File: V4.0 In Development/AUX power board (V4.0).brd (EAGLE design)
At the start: 100 x 100 mm, 96 parts, among them U1 ATMEGA328P_TQFP, U2 TPS5405DR

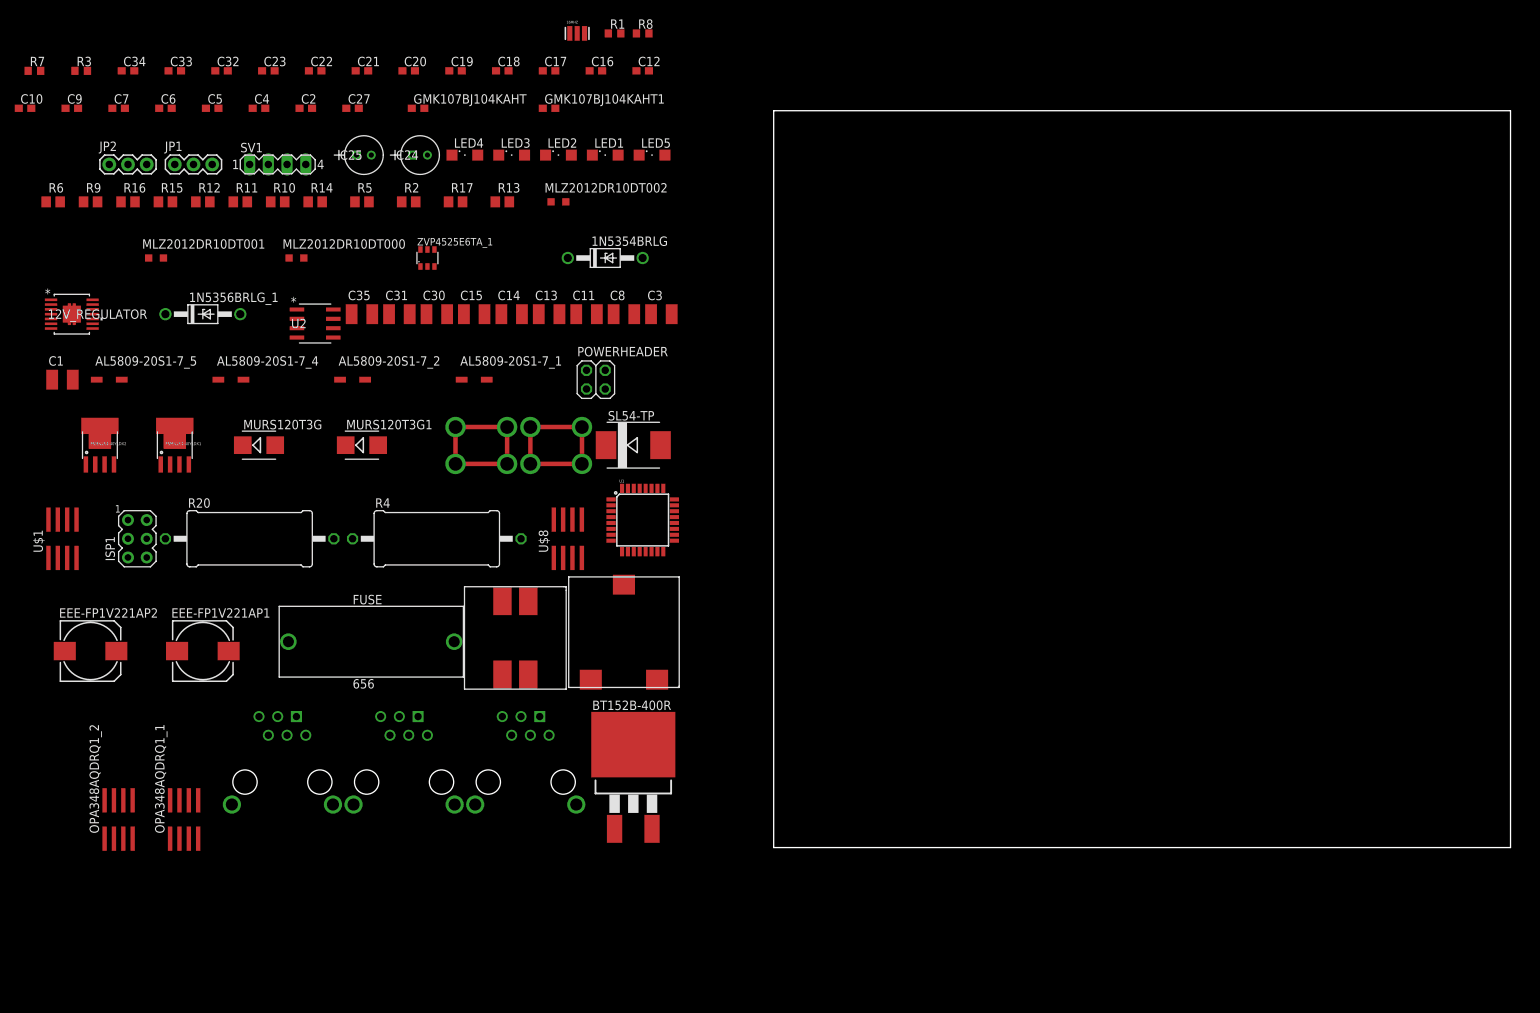
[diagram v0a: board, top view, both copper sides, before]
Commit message: Generated the board file
-Generated Board files
-Sorted the components
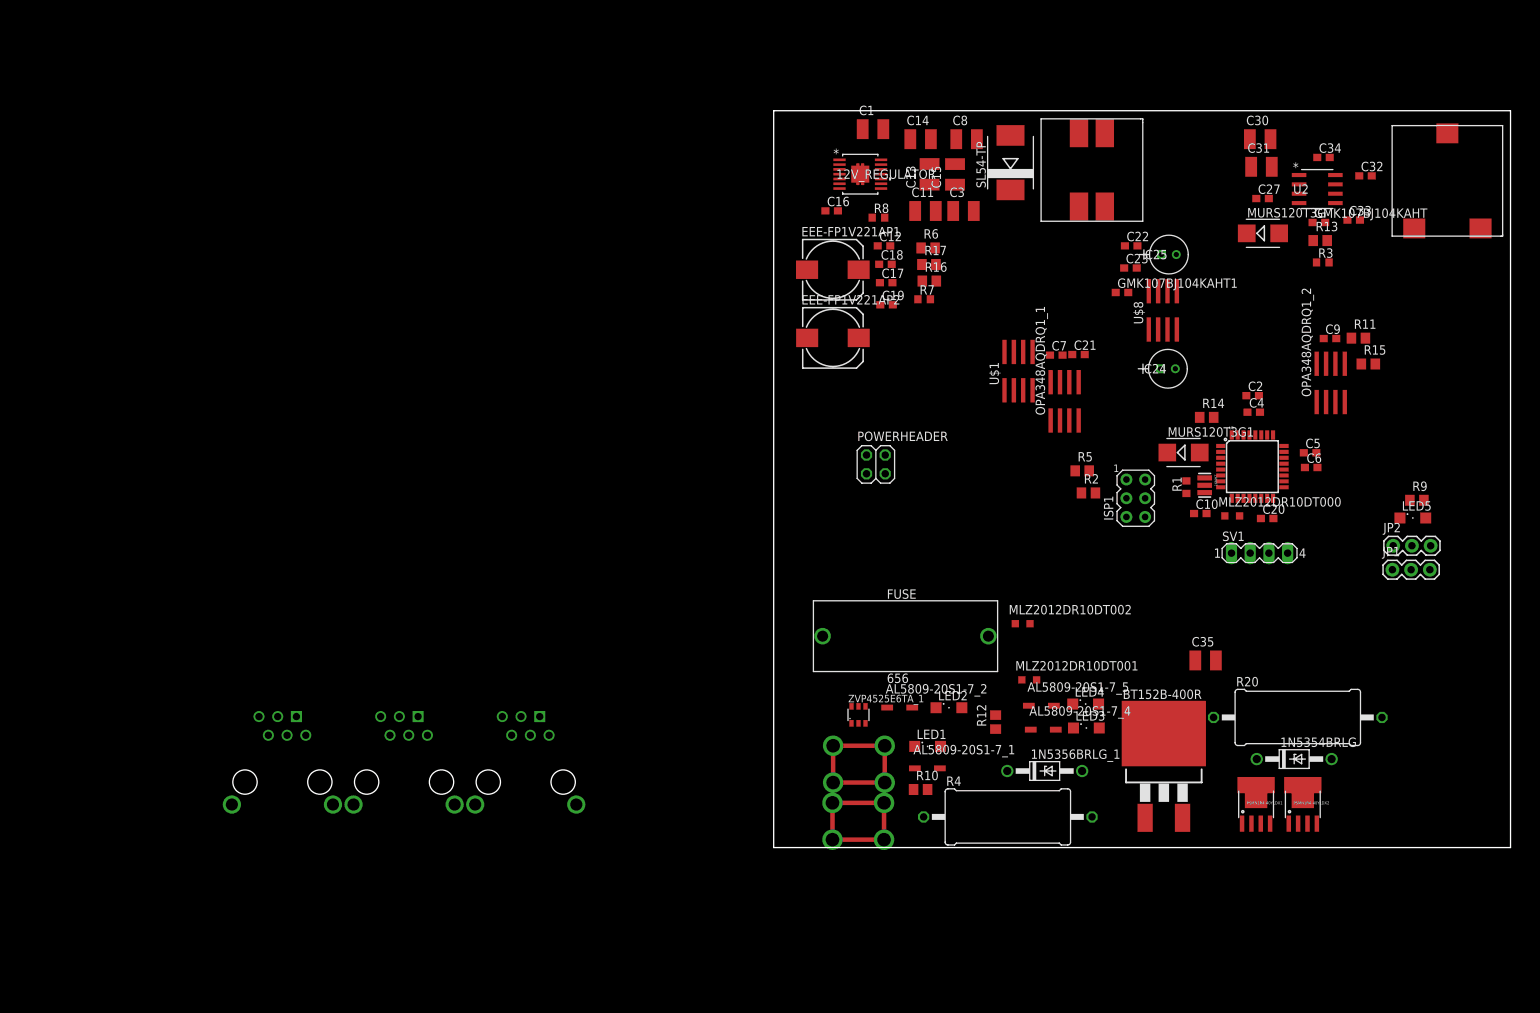
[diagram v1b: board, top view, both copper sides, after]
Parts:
- moved R9 184.5 mm to (87.3, 47.1)
- moved JP2 181.8 mm to (84.1, 41.0)
- moved OPA348AQDRQ1_2 174.8 mm to (75.6, 63.1)
- moved JP1 174.2 mm to (84.0, 37.7)
- moved C9 173.6 mm to (75.5, 69.1)
- moved R3 170.5 mm to (74.5, 79.4)
- moved PSMN1R4-40YLDX2 170.4 mm to (71.8, 5.86)
- moved C10 168.7 mm to (57.9, 45.3)
- moved R15 164.7 mm to (80.7, 65.6)
- moved C6 163.0 mm to (73.0, 51.6)
- moved C34 162.7 mm to (74.6, 93.7)
- moved C33 161.3 mm to (78.7, 85.2)
- moved C5 156.2 mm to (72.8, 53.6)
- moved C32 155.9 mm to (80.3, 91.2)
- moved PSMN1R4-40YLDX1 154.6 mm to (65.5, 5.86)
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
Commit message: Worked on PCB (Input)
-Not complete
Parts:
- moved U$3 108.0 mm to (75.0, 11.7)
- moved U$4 107.0 mm to (57.5, 11.7)
- moved U$10 106.0 mm to (40.0, 11.7)
- moved U$7 80.0 mm to (88.0, 5.00)
- moved LED4 69.5 mm to (-24.7, 38.0)
- moved AL5809-20S1-7_5 68.9 mm to (-26.7, -8.75)
- moved C35 68.6 mm to (-6.38, 3.39)
- moved R12 61.8 mm to (-30.4, 29.5)
- moved LED3 61.0 mm to (-18.6, 17.7)
- moved R4 59.0 mm to (-27.2, 2.66)
- moved MLZ2012DR10DT001 55.5 mm to (-20.8, 24.3)
- moved 1N5356BRLG_1 54.0 mm to (-17.2, 10.4)
- moved R10 49.7 mm to (-29.6, 12.4)
- moved AL5809-20S1-7_4 49.5 mm to (-8.91, -3.50)
- moved MLZ2012DR10DT002 46.2 mm to (-11.7, 22.4)
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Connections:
- net GND: no longer U$10.SH1, U$10.SH2, U$3.SH1, U$3.SH2, U$4.SH1, U$4.SH2
- net NEG_TERMINAL: now also U$10.SH1, U$10.SH2, U$3.SH1, U$3.SH2, U$4.SH1, U$4.SH2
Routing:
- net NEG_TERMINAL: track 0.00 -> 164.9 mm
- net INPUT_UNREG: track 0.00 -> 61.6 mm, vias 0 -> 3
- net N$17: track 0.00 -> 15.8 mm, vias 0 -> 1
- net BATTERY_IN_UNFUSED+: track 0.00 -> 11.4 mm
- net N$25: track 0.00 -> 2.77 mm
- net N$22: track 0.00 -> 2.63 mm
- added copper zone on layer 1, net GND
- added copper zone on layer 16, net GND

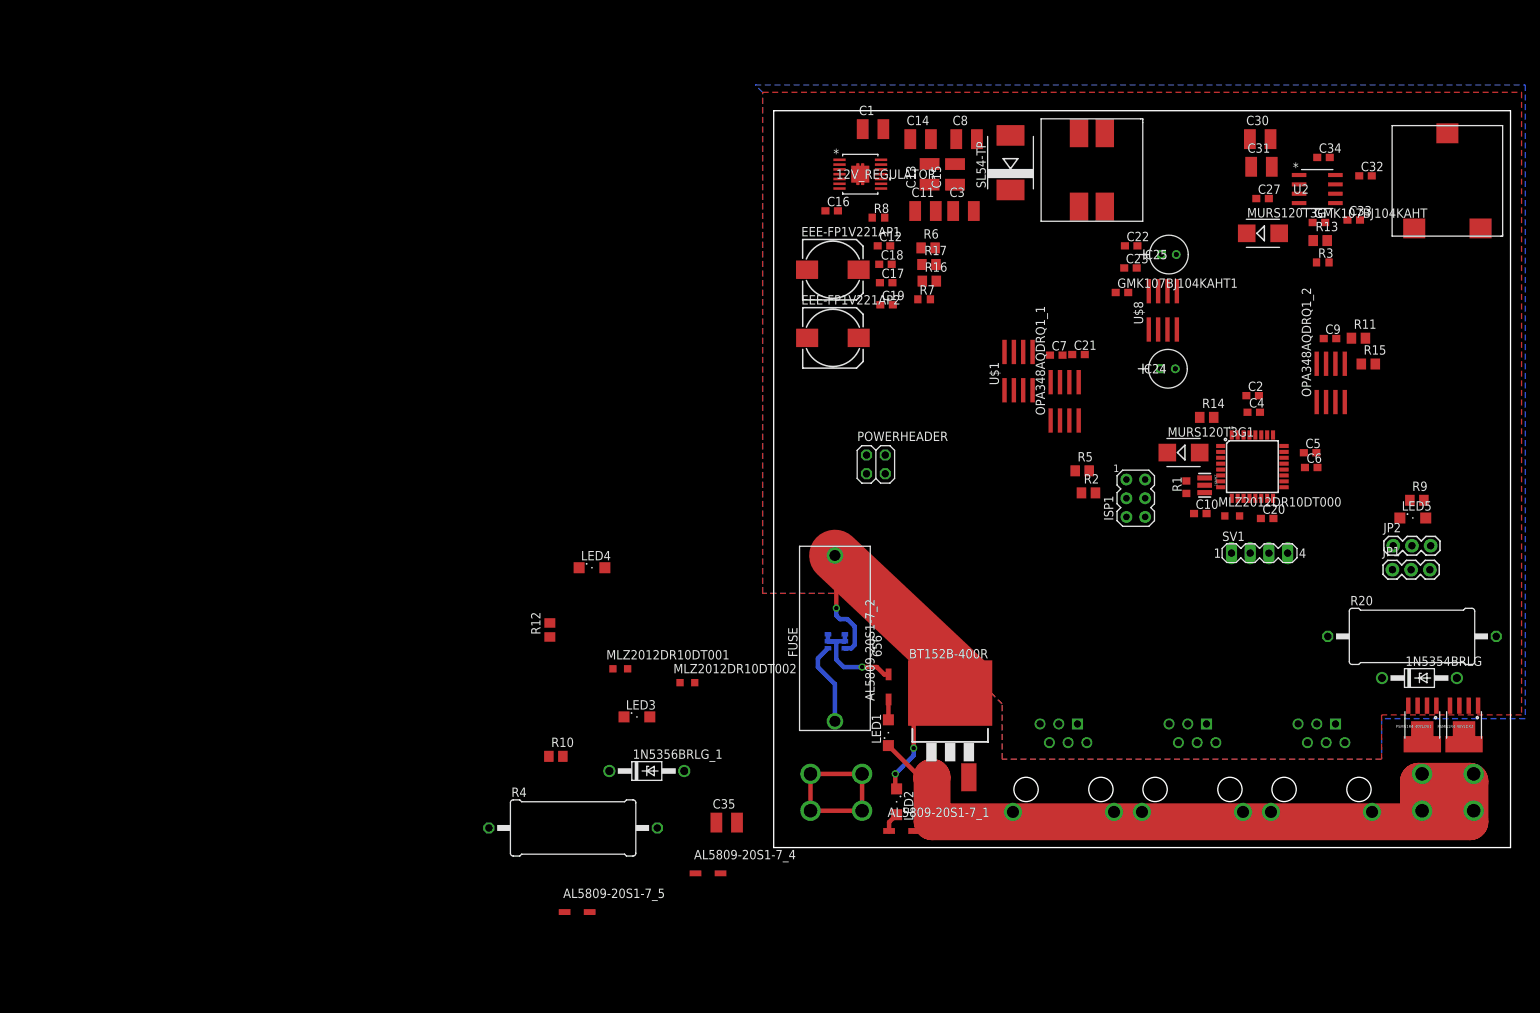
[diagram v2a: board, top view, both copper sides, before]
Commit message: Deleted -12V REG and op-amps
They add complexity/expense/risk without adding much performance.

When testing the -12V on the motor controller, the performance was poor. I am too lazy to re-spec a part so its much more efficient on time to just remove it.
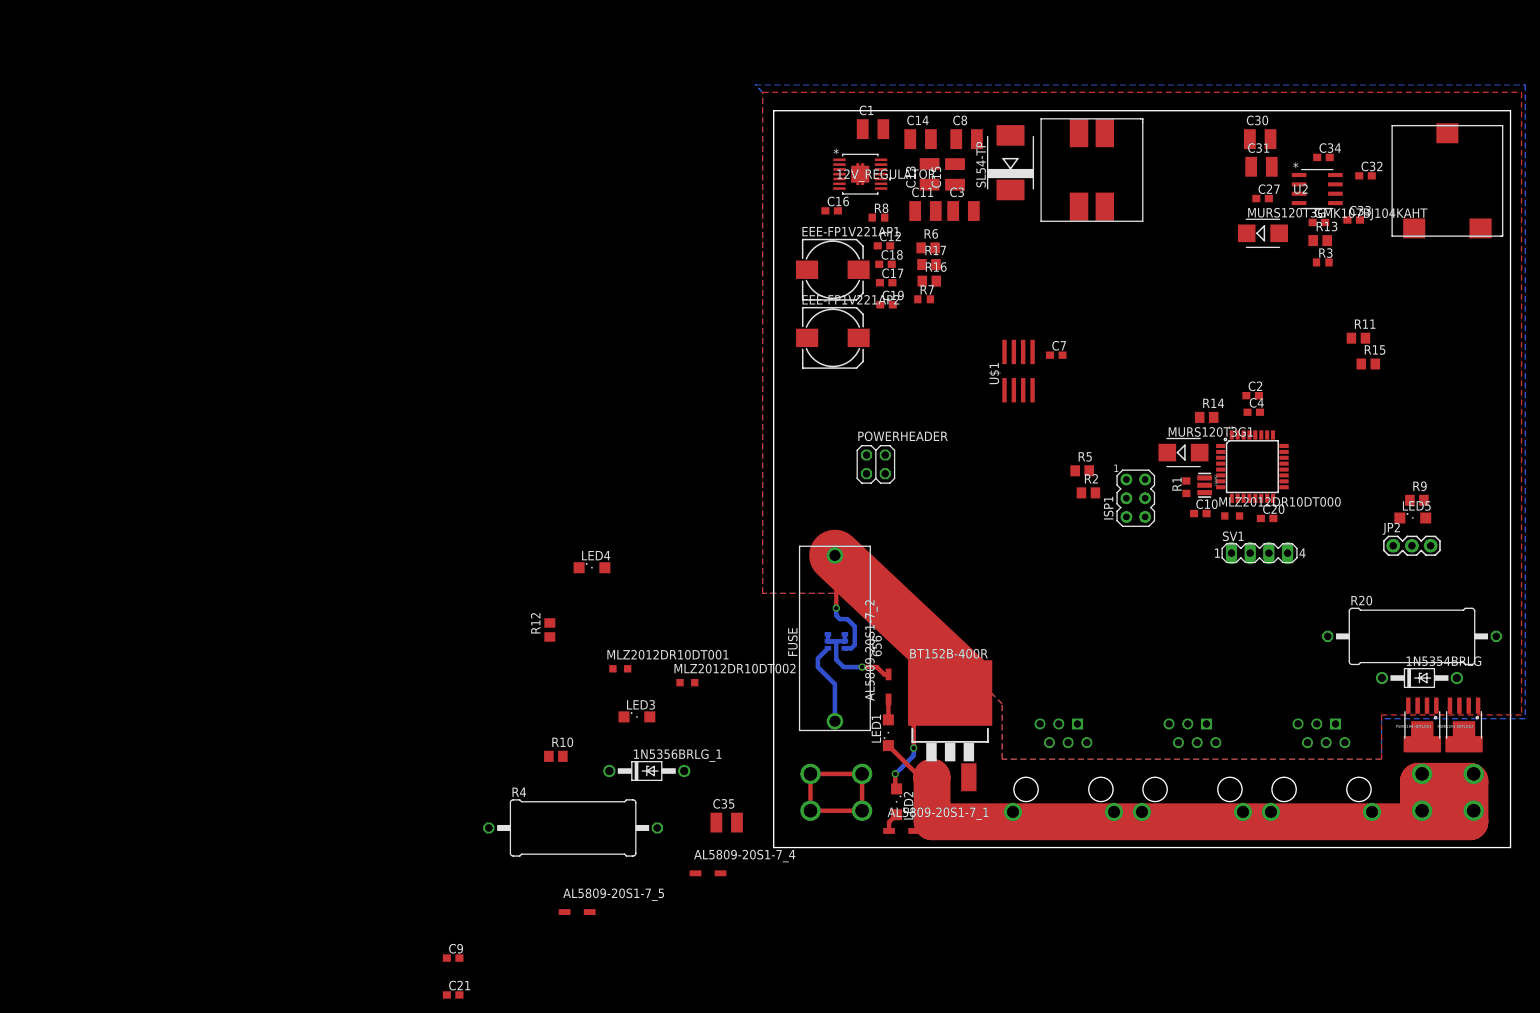
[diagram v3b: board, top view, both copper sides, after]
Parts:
- removed C22, C23, C6: 2.2uF, rcl:C0603
- removed C24, C25: UPJ1V220MDD1TD, UPJ1V220MDD1TD:U1-E
- removed C5, GMK107BJ104KAHT1: 0.1uF, rcl:C0603
- removed JP1: (no value), SparkFun (2015_10_14 22_27_04 UTC):1X03
- removed OPA348AQDRQ1_1, OPA348AQDRQ1_2: OPA344U, linear:SO08
- removed U$8: ICL7662CBA, linear:SO08
- moved C9 145.7 mm to (-43.5, -15.0)
- moved C21 121.5 mm to (-43.5, -20.0)
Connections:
- removed net DATA_LOG_INPUT_12V: OPA348AQDRQ1_2.7
- removed net DATA_LOG_POWER_12V: C22.1, GMK107BJ104KAHT1.1, JP1.2, OPA348AQDRQ1_1.7, U$8.8
- removed net N$11: C24.2, U$8.4
- removed net N$12: OPA348AQDRQ1_2.3, R11.1, R15.2
- removed net N$16: C24.1, U$8.2
- removed net N$2: OPA348AQDRQ1_1.3, U$1.7
- removed net OUTPUT_12NEG: C23.1, C25.2, OPA348AQDRQ1_1.4, OPA348AQDRQ1_2.4, U$8.5
- new net I_MEASUREMENT: C21.1, U$1.7, U1.23
- new net V_MEASURMENT: C9.1, R11.1, R15.2
- net BATTERY_V(0-5): no longer C9.1, OPA348AQDRQ1_2.2, OPA348AQDRQ1_2.6
- net GND: no longer C22.2, C25.1, C5.2, C6.2, GMK107BJ104KAHT1.2, JP1.3, U$8.1, U$8.3, U$8.6
- net I_MEASUREMENT_OUT: no longer C21.1, C5.1, C6.1, OPA348AQDRQ1_1.2, OPA348AQDRQ1_1.6, U1.23
- net OUTPUT_12REG: no longer JP1.1
